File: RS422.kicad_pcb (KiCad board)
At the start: 2 copper layers, 30 x 41.5 mm, 12 parts, among them J1 L77SDA15S1ACH4F, J2 Conn_01x05_Male, J3 Conn_01x05_Male, J4 Conn_01x01_Male, U1 AM26LV32xD, U2 AM26LV32xD

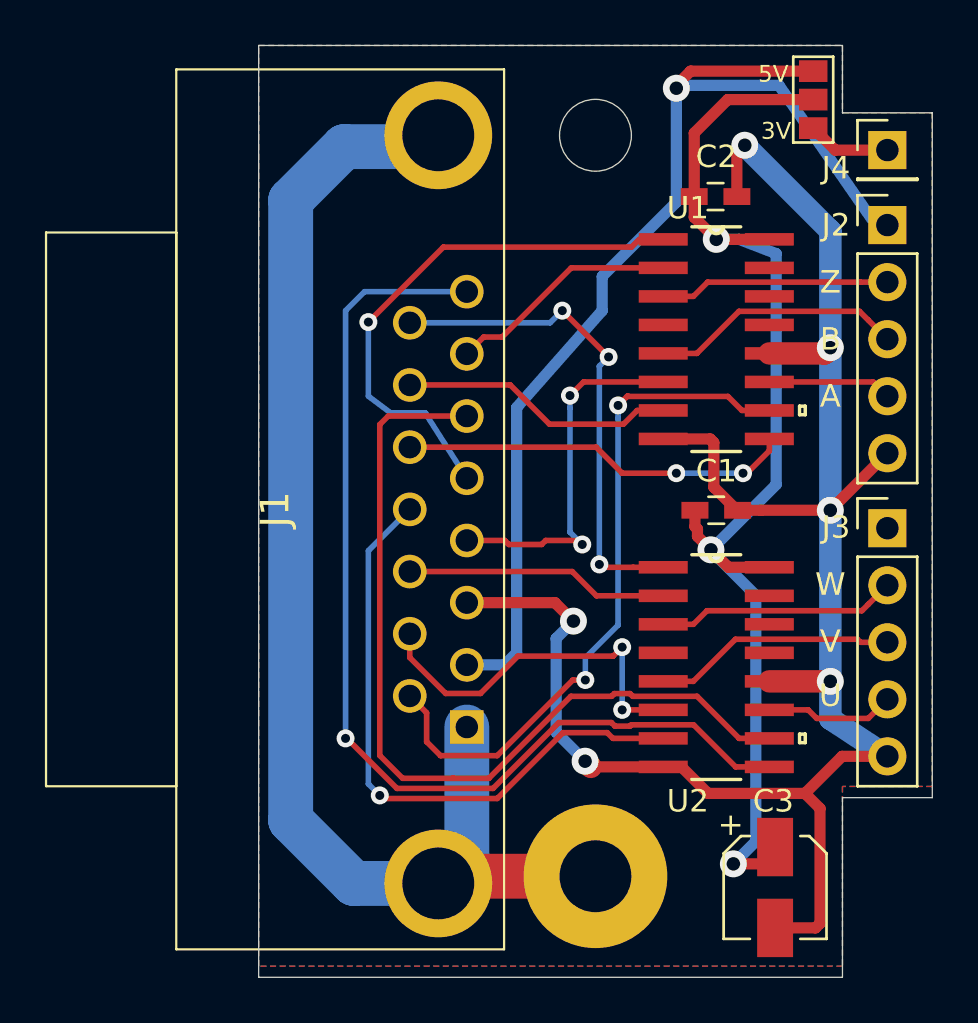
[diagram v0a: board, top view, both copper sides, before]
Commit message: Updated README & Silkscreen mods
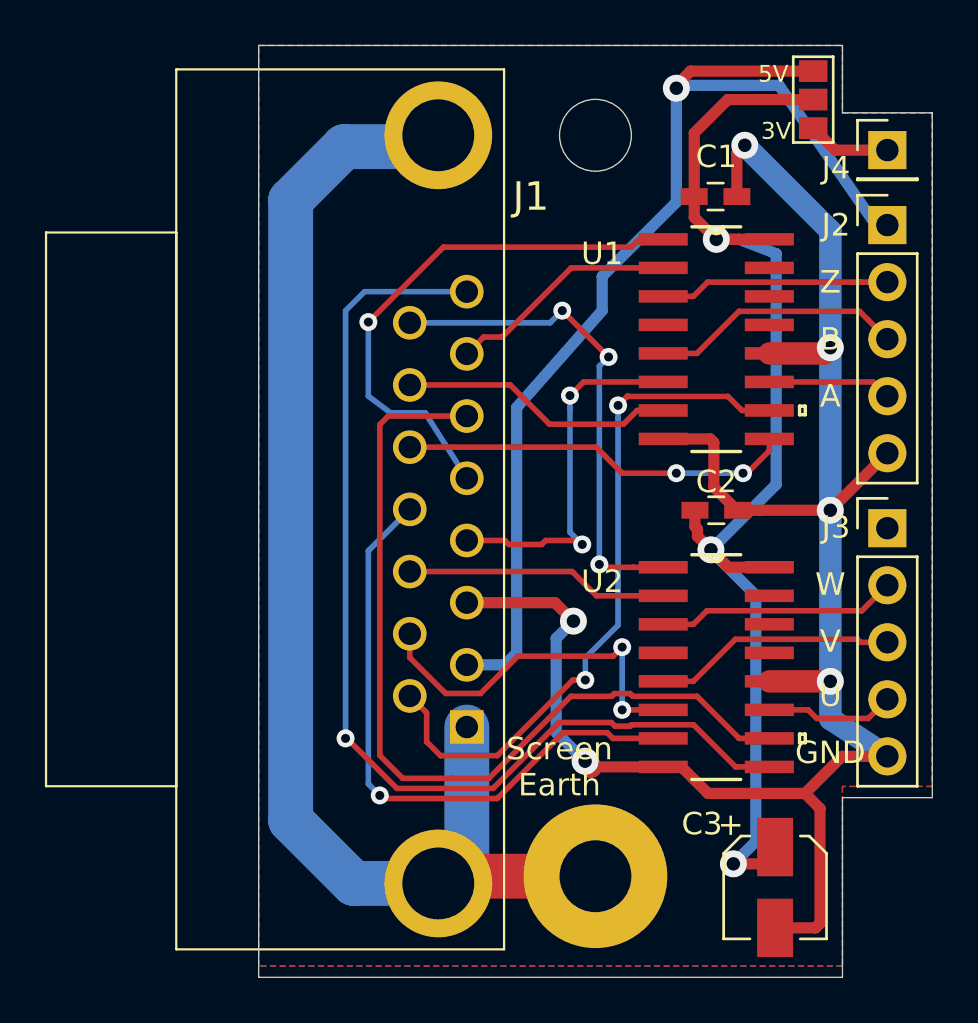
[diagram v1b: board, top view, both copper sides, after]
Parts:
- added REF***: KiCad-Logo2_6mm_SilkScreen, Symbols:KiCad-Logo2_6mm_SilkScreen, B.Cu at (121.3, 87.0)
- added REF***: OSHW-Logo2_9.8x8mm_SilkScreen, Symbols:OSHW-Logo2_9.8x8mm_SilkScreen, B.Cu at (121.9, 73.0)
- renumbered C2 to C1, C1 to C2
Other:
- board text added: "GND"
- board text added: "Screen Earth"

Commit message: Clean up ignored files
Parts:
- moved REF*** 10.3 mm to (128.3, 94.6)
- moved REF*** 8.54 mm to (127.6, 66.7)
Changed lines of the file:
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@@
   (page A4)
   (layers
-    (0 F.Cu signal hide)
-    (31 B.Cu signal hide)
+    (0 F.Cu signal)
+    (31 B.Cu signal)
     (32 B.Adhes user)
     (33 F.Adhes user)
@@
     (38 B.Mask user)
     (39 F.Mask user)
-    (40 Dwgs.User user hide)
-    (41 Cmts.User user hide)
+    (40 Dwgs.User user)
+    (41 Cmts.User user)
     (42 Eco1.User user)
     (43 Eco2.User user)
@@
     (45 Margin user)
     (46 B.CrtYd user)
-    (47 F.CrtYd user hide)
+    (47 F.CrtYd user)
     (48 B.Fab user)
     (49 F.Fab user)
@@
       (viasonmask false)
       (mode 1)
-      (useauxorigin false)
+      (useauxorigin true)
       (hpglpennumber 1)
       (hpglpenspeed 20)
@@
       (drillshape 0)
       (scaleselection 1)
-      (outputdirectory "./"))
+      (outputdirectory "./Plots"))
   )
   (net 0 "")
@@
   )
   (module Symbols:KiCad-Logo2_6mm_SilkScreen (layer B.Cu)
-    (at 121.285 86.995 270)
+    (at 128.27 94.615 270)
     (descr "KiCad Logo")
     (tags "Logo KiCad")
@@
   )
   (module Symbols:OSHW-Logo2_9.8x8mm_SilkScreen (layer B.Cu)
-    (at 121.92 73.025 270)
+    (at 127.635 66.675 270)
     (descr "Open Source Hardware Symbol")
     (tags "Logo Symbol OSHW")
@@
     (effects (font (size 1 1) (thickness 0.15)))
   )
-  (gr_text "Open FFBoard\nDifferential Motor Encoder Interface\nv1.0 - Jon Lidgard 2020" (at 129.54 79.58 90) (layer B.SilkS)
+  (gr_text "Open FFBoard\nDifferential Motor Encoder Interface\nv1.0 - Jon Lidgard 2020" (at 120.65 80.01 90) (layer B.SilkS)
     (effects (font (size 1 1) (thickness 0.15)) (justify mirror))
   )
